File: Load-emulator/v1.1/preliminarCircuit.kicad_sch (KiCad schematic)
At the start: 4 parts, among them J4 533980771, J5 532610471, J6 532610471, J7 532610471

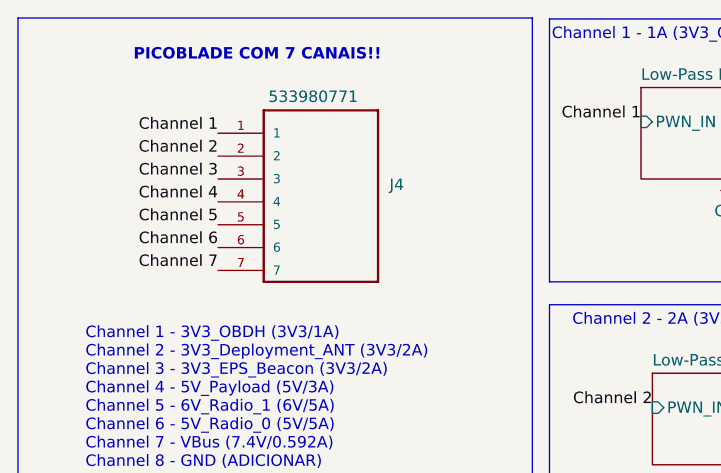
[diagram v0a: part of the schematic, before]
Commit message: changes in lib- add new connectors
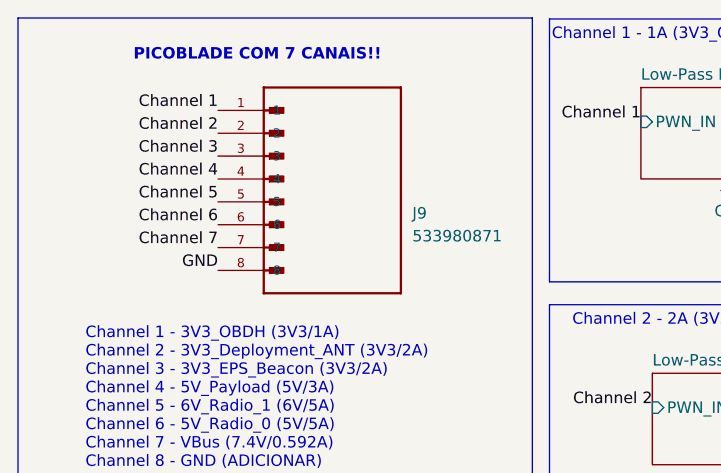
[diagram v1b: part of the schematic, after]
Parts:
- removed J4: 533980771, Connector_Molex:Molex_PicoBlade_53398-0771_1x07-1MP_P1.25mm_Vertical, symbol 533980771:533980771
- added J9: 533980871, footprints:MOLEX_533980871, symbol 533980871:533980871
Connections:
- net Channel 1: now also J9.1
- net Channel 2: now also J9.2
- net Channel 3: now also J9.3
- net Channel 4: now also J9.4
- net Channel 5: now also J9.5
- net Channel 6: now also J9.6
- net Channel 7: now also J9.7
- net GND: now also J9.8
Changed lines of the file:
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@@
+		)
+	)
+	(label "GND"
+		(at 36.83 41.91 180)
+		(effects
+			(font
+				(size 1.27 1.27)
+			)
+			(justify right bottom)
 		)
 	)
 	(label "Channel 7"
-		(at 36.83 41.91 180)
+		(at 36.83 39.37 180)
 		(effects
 			(font
@@
 	)
 	(label "Channel 2"
-		(at 36.83 29.21 180)
+		(at 36.83 26.67 180)
 		(effects
 			(font
@@
 	)
 	(label "Channel 5"
-		(at 36.83 36.83 180)
+		(at 36.83 34.29 180)
 		(effects
 			(font
@@
 	)
 	(label "Channel 4"
-		(at 36.83 34.29 180)
+		(at 36.83 31.75 180)
 		(effects
 			(font
@@
 	)
 	(label "Channel 6"
-		(at 36.83 39.37 180)
+		(at 36.83 36.83 180)
 		(effects
 			(font
@@
 	)
 	(label "Channel 1"
-		(at 36.83 26.67 180)
+		(at 36.83 24.13 180)
 		(effects
 			(font
@@
 	)
 	(label "Channel 3"
-		(at 36.83 31.75 180)
+		(at 36.83 29.21 180)
 		(effects
 			(font
@@
 	)
 	(symbol
-		(lib_id "533980771:533980771")
-		(at 48.26 35.56 0)
-		(unit 1)
-		(exclude_from_sim no)
-		(in_bom yes)
-		(on_board yes)
-		(dnp no)
-		(property "Reference" "J4"
-			(at 55.88 32.3849 0)
-			(effects
-				(font
-					(size 1.27 1.27)
-				)
-				(justify left)
-			)
-		)
-		(property "Value" "533980771"
-			(at 42.418 22.606 0)
-			(effects
-				(font
-					(size 1.27 1.27)
-				)
-				(justify left)
-			)
-		)
-		(property "Footprint" "Connector_Molex:Molex_PicoBlade_53398-0771_1x07-1MP_P1.25mm_Vertical"
-			(at 65.024 84.582 0)
-			(effects
-				(font
-					(size 1.27 1.27)
-				)
-				(justify bottom)
-				(hide yes)
-			)
-		)
-		(property "Datasheet" ""
-			(at 48.26 35.56 0)
-			(effects
-				(font
-					(size 1.27 1.27)
-				)
-				(hide yes)
-			)
-		)
-		(property "Description" ""
-			(at 48.26 35.56 0)
-			(effects
-				(font
-					(size 1.27 1.27)
-				)
-				(hide yes)
-			)
-		)
-		(property "MF" "Molex"
-			(at 81.788 48.26 0)
-			(effects
-				(font
-					(size 1.27 1.27)
-				)
-				(justify bottom)
-				(hide yes)
-			)
-		)
-		(property "MAXIMUM_PACKAGE_HEIGHT" "4.7 mm"
-			(at 65.532 33.528 0)
-			(effects
-				(font
-					(size 1.27 1.27)
-				)
-				(justify bottom)
-				(hide yes)
-			)
-		)
-		(property "Package" "None"
-			(at 65.024 29.21 0)
-			(effects
-				(font
-					(size 1.27 1.27)
-				)
-				(justify bottom)
-				(hide yes)
-			)
-		)
-		(property "Price" "None"
-			(at 68.326 27.432 0)
-			(effects
-				(font
-					(size 1.27 1.27)
-				)
-				(justify bottom)
-				(hide yes)
-			)
-		)
-		(property "Check_prices" "https://www.snapeda.com/parts/533980771/Molex/view-part/?ref=eda"
-			(at 67.818 90.424 0)
-			(effects
-				(font
-					(size 1.27 1.27)
-				)
-				(justify bottom)
-				(hide yes)
-			)
-		)
-		(property "STANDARD" "Manufacturer Recommendations"
-			(at 92.964 44.196 0)
-			(effects
-				(font
-					(size 1.27 1.27)
-				)
-				(justify bottom)
-				(hide yes)
-			)
-		)
-		(property "PARTREV" "A"
-			(at 64.262 24.384 0)
-			(effects
-				(font
-					(size 1.27 1.27)
-				)
-				(justify bottom)
-				(hide yes)
-			)
-		)
-		(property "SnapEDA_Link" "https://www.snapeda.com/parts/533980771/Molex/view-part/?ref=snap"
-			(at 50.292 74.93 0)
-			(effects
-				(font
-					(size 1.27 1.27)
-				)
-				(justify bottom)
-				(hide yes)
-			)
-		)
-		(property "MP" "533980771"
-			(at 80.518 47.498 0)
-			(effects
-				(font
-					(size 1.27 1.27)
-				)
-				(justify bottom)
-				(hide yes)
-			)
-		)
-		(property "Description_1" "\n                        \n                            Conn Shrouded Header (3 Sides) HDR 7 POS 1.25mm Solder ST Top Entry SMD PicoBlade™ T/R\n                        \n"
-			(at 48.006 67.564 0)
-			(effects
-				(font
-					(size 1.27 1.27)
-				)
-				(justify bottom)
-				(hide yes)
-			)
-		)
-		(property "Availability" "In Stock"
-			(at 74.168 59.436 0)
-			(effects
-				(font
-					(size 1.27 1.27)
-				)
-				(justify bottom)
-				(hide yes)
-			)
-		)
-		(property "MANUFACTURER" "Molex"
-			(at 65.024 34.544 0)
-			(effects
-				(font
-					(size 1.27 1.27)
-				)
-				(justify bottom)
-				(hide yes)
-			)
-		)
-		(pin "6"
-		)
-		(pin "5"
-		)
-		(pin "1"
-		)
-		(pin "2"
-		)
-		(pin "3"
-		)
-		(pin "4"
-		)
-		(pin "7"
-		)
-		(instances
-			(project ""
-				(path "/9054bfd2-3cc0-4c96-aa71-abdb09b76dc7/a12c045f-372a-4c5b-93d1-0c234b5f9c5c"
-					(reference "J4")
-					(unit 1)
-				)
-			)
-		)
-	)
-	(symbol
 		(lib_id "power:GND")
 		(at 113.03 176.53 0)
@@
 					(unit 1)
 				)
+			)
+		)
+	)
+	(symbol
+		(lib_id "533980871:533980871")
+		(at 49.53 36.83 0)
+		(unit 1)
+		(exclude_from_sim no)
+		(in_bom yes)
+		(on_board yes)
+		(dnp no)
+		(fields_autoplaced yes)
+		(property "Reference" "J9"
+			(at 58.42 35.5599 0)
+			(effects
+				(font
+					(size 1.27 1.27)
+				)
+				(justify left)
+			)
+		)
+		(property "Value" "533980871"
+			(at 58.42 38.0999 0)
+			(effects
+				(font
+					(size 1.27 1.27)
+				)
+				(justify left)
+			)
+		)
+		(property "Footprint" "footprints:MOLEX_533980871"
+			(at 61.976 1.778 0)
+			(effects
+				(font
+					(size 1.27 1.27)
+				)
+				(justify bottom)
+				(hide yes)
+			)
+		)
+		(property "Datasheet" ""
+			(at 49.53 36.83 0)
+			(effects
+				(font
+					(size 1.27 1.27)
+				)
+				(hide yes)
+			)
+		)
+		(property "Description" ""
+			(at 49.53 36.83 0)
+			(effects
+				(font
+					(size 1.27 1.27)
+				)
+				(hide yes)
+			)
+		)
+		(property "MF" "Molex"
+			(at 68.072 -7.874 0)
+			(effects
+				(font
+					(size 1.27 1.27)
+				)
+				(justify bottom)
+				(hide yes)
+			)
+		)
+		(property "MAXIMUM_PACKAGE_HEIGHT" "4.7 mm"
+			(at 57.15 1.778 0)
+			(effects
+				(font
+					(size 1.27 1.27)
+				)
+				(justify bottom)
+				(hide yes)
+			)
+		)
+		(property "Package" "None"
+			(at 71.882 -7.112 0)
+			(effects
+				(font
+					(size 1.27 1.27)
+				)
+				(justify bottom)
+				(hide yes)
+			)
+		)
+		(property "Price" "None"
+			(at 51.562 -0.508 0)
+			(effects
+				(font
+					(size 1.27 1.27)
+				)
+				(justify bottom)
+				(hide yes)
+			)
+		)
+		(property "Check_prices" "https://www.snapeda.com/parts/533980871/Molex/view-part/?ref=eda"
+			(at 35.052 -0.254 0)
+			(effects
+				(font
+					(size 1.27 1.27)
+				)
+				(justify bottom)
+				(hide yes)
+			)
+		)
+		(property "STANDARD" "Manufacturer Recommendations"
+			(at 60.452 -0.254 0)
+			(effects
+				(font
+					(size 1.27 1.27)
+				)
+				(justify bottom)
+				(hide yes)
+			)
+		)
+		(property "PARTREV" "A"
+			(at 54.356 6.604 0)
+			(effects
+				(font
+					(size 1.27 1.27)
+				)
+				(justify bottom)
+				(hide yes)
+			)
+		)
+		(property "SnapEDA_Link" "https://www.snapeda.com/parts/533980871/Molex/view-part/?ref=snap"
+			(at 35.052 -0.254 0)
+			(effects
+				(font
+					(size 1.27 1.27)
+				)
+				(justify bottom)
+				(hide yes)
+			)
+		)
+		(property "MP" "533980871"
+			(at 52.832 4.572 0)
+			(effects
+				(font
+					(size 1.27 1.27)
+				)
+				(justify bottom)
+				(hide yes)
+			)
+		)
+		(property "Description_1" "Connector Header Surface Mount 8 position 0.049 (1.25mm)"
+			(at 35.052 -0.254 0)
+			(effects
+				(font
+					(size 1.27 1.27)
+				)
+				(justify bottom)
+				(hide yes)
+			)
+		)
+		(property "Availability" "In Stock"
+			(at 55.118 3.556 0)
+			(effects
+				(font
+					(size 1.27 1.27)
+				)
+				(justify bottom)
+				(hide yes)
+			)
+		)
+		(property "MANUFACTURER" "Molex"
+			(at 66.294 -7.62 0)
+			(effects
+				(font
+					(size 1.27 1.27)
+				)
+				(justify bottom)
+				(hide yes)
+			)
+		)
+		(pin "4"
+		)
+		(pin "6"
+		)
+		(pin "1"
+		)
+		(pin "2"
+		)
+		(pin "3"
+		)
+		(pin "5"
+		)
+		(pin "8"
+		)
+		(pin "7"
+		)
+		(instances
+			(project "Load-emulator"
+				(path "/9054bfd2-3cc0-4c96-aa71-abdb09b76dc7/a12c045f-372a-4c5b-93d1-0c234b5f9c5c"
+					(reference "J9")
+					(unit 1)
+				)

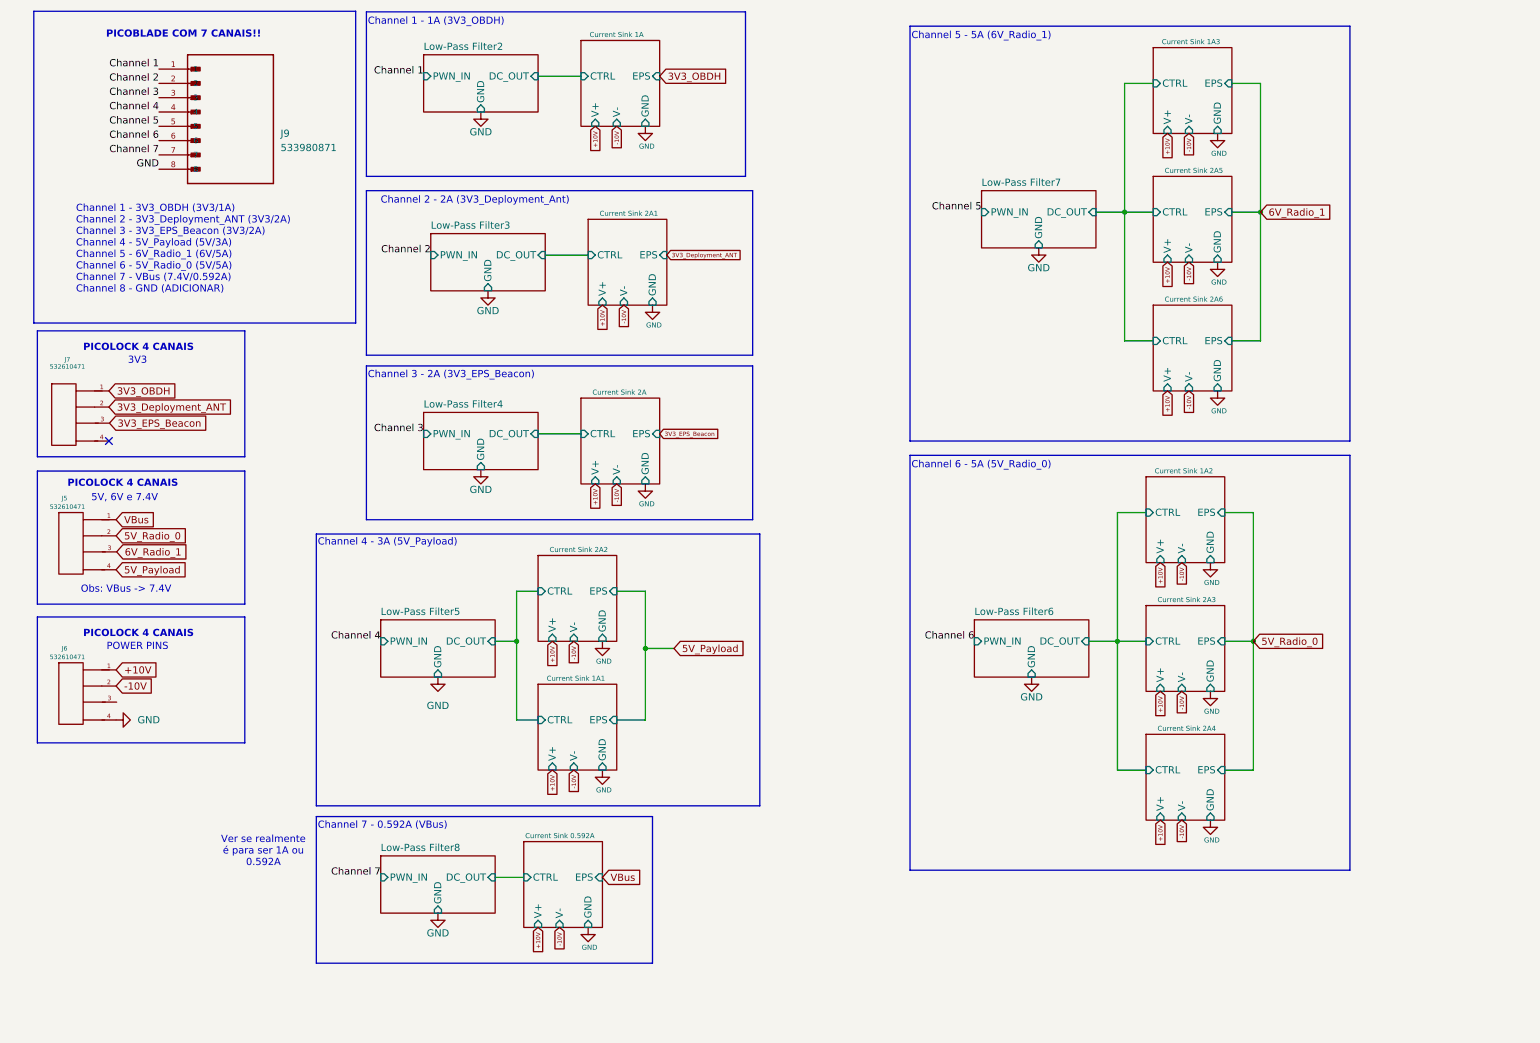
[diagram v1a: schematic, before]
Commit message: Channels reduced to 3A max
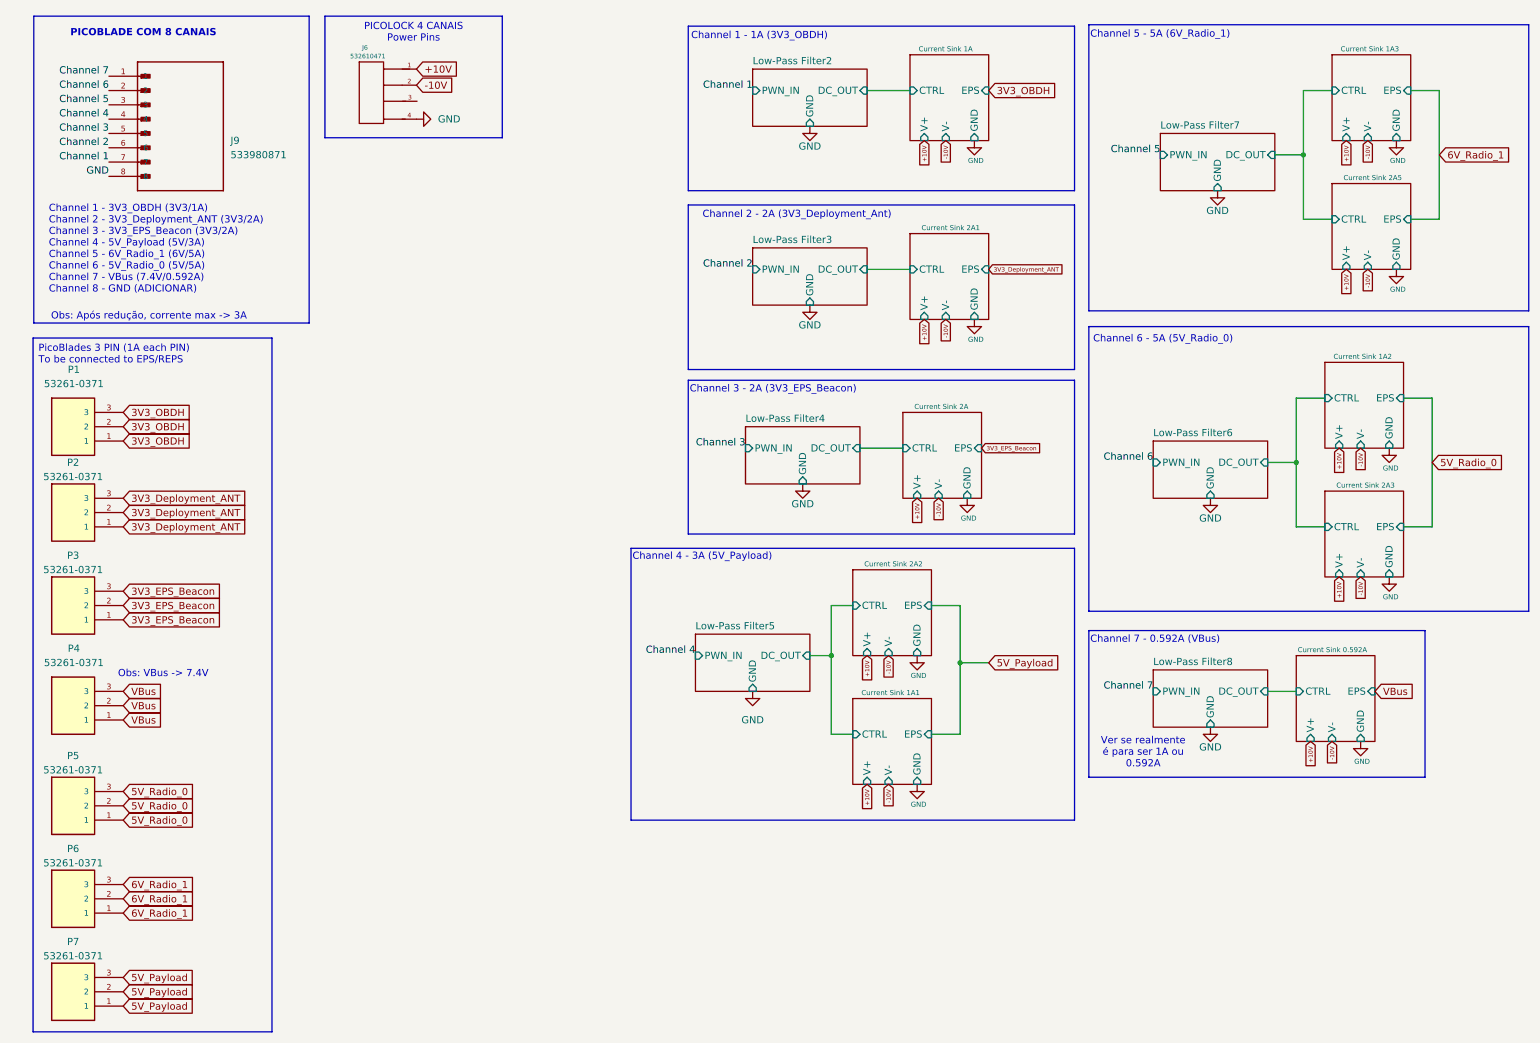
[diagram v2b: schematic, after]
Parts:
- removed J5, J7: 532610471, footprints:532610471, symbol 532610471:532610471
- added P1, P2, P3, P4, P5, P6, P7: 53261-0371, footprints:MOLEX_53261-0371, symbol 53261-0371:53261-0371
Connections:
- net 3V3_Deployment_ANT: now also P2.1, P2.2, P2.3
- net 3V3_EPS_Beacon: now also P3.1, P3.2, P3.3
- net 3V3_OBDH: now also P1.1, P1.2, P1.3
- net 5V_Payload: now also P7.1, P7.2, P7.3
- net 5V_Radio_0: now also P5.1, P5.2, P5.3
- net 6V_Radio_1: now also P6.1, P6.2, P6.3
- net Channel 1: now also J9.7; no longer J9.1
- net Channel 2: now also J9.6; no longer J9.2
- net Channel 3: now also J9.5; no longer J9.3
- net Channel 5: now also J9.3; no longer J9.5
- net Channel 6: now also J9.2; no longer J9.6
- net Channel 7: now also J9.1; no longer J9.7
- net VBus: now also P4.1, P4.2, P4.3
- no-connect marks 1 -> 0
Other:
- removed sheet Current Sink 2A4
- removed sheet Current Sink 2A6
- note added: "Obs: Após redução, corrente max -> 3A"
- note added: "PICOBLADE COM 8 CANAIS"
- note removed: "3V3"
- note removed: "5V, 6V e 7.4V"
- note removed: "PICOBLADE COM 7 CANAIS!!"
- note removed: "PICOLOCK 4 CANAIS"
- note removed: "POWER PINS"
- moved on the sheet: J6, J9

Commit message: Foram adicionados todos os canais, removidos os pinos de conexao para o REPS, foram feitas todas as trilhas de potência, controle e alimentação, com exceção do GND.
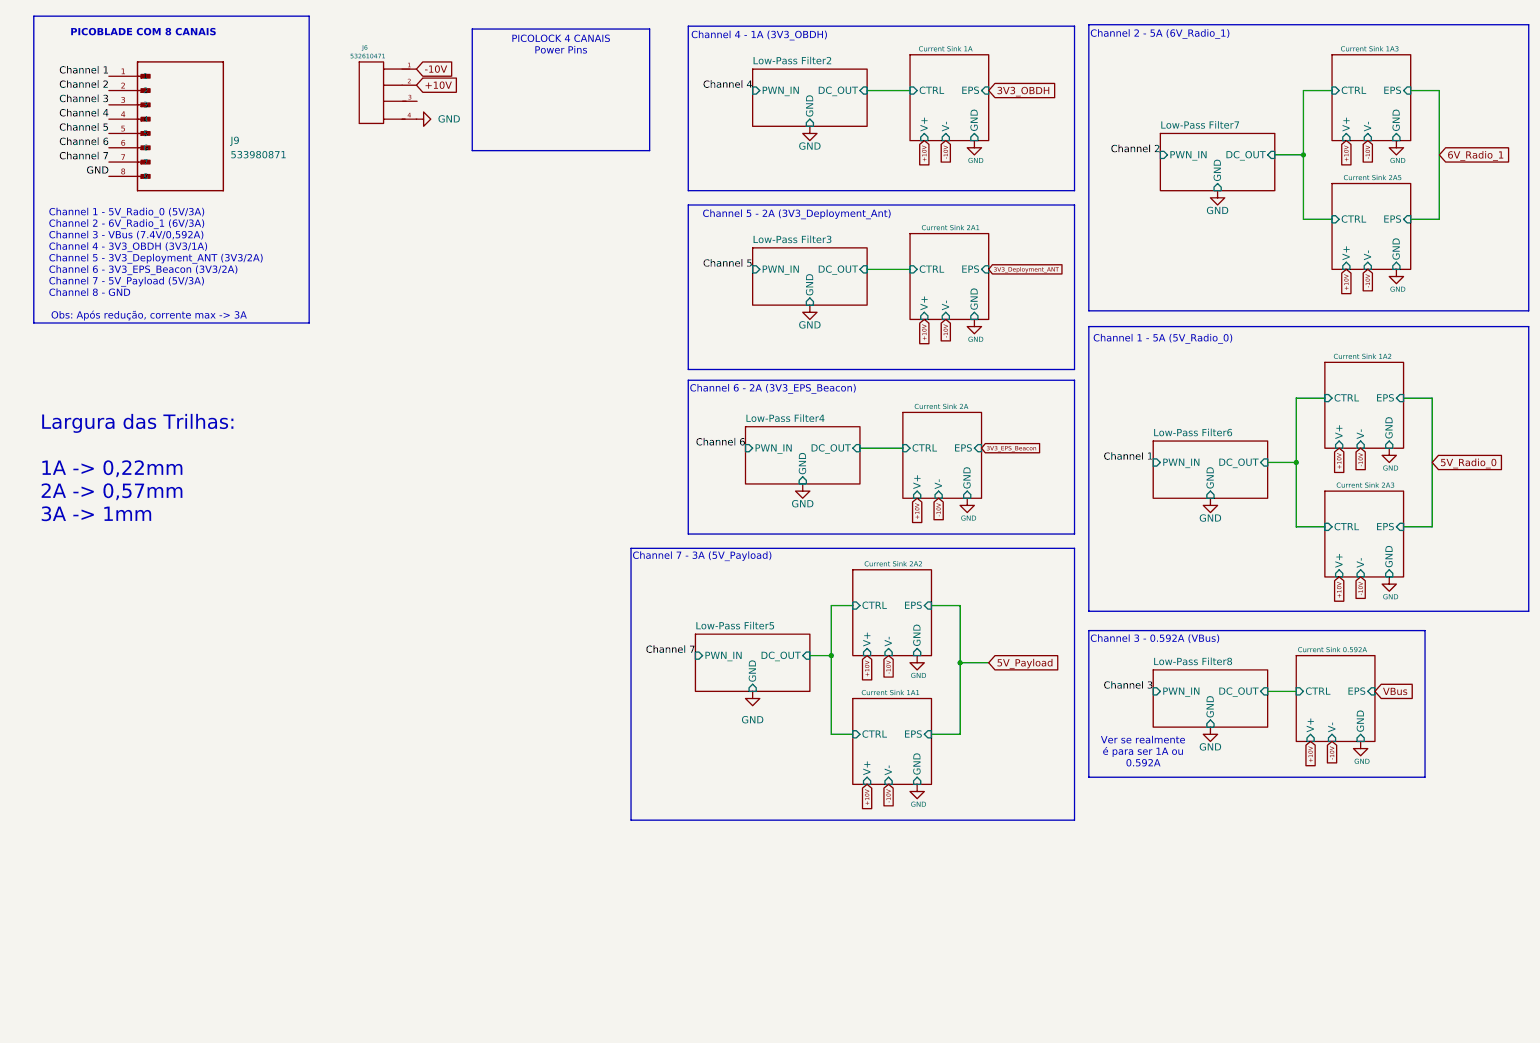
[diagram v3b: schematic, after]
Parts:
- removed P1, P2, P3, P4, P5, P6, P7: 53261-0371, footprints:MOLEX_53261-0371, symbol 53261-0371:53261-0371
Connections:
- net +10V: now also J6.2; no longer J6.1
- net -10V: now also J6.1; no longer J6.2
- net Channel 1: now also J9.1; no longer J9.7
- net Channel 2: now also J9.2; no longer J9.6
- net Channel 3: now also J9.3; no longer J9.5
- net Channel 5: now also J9.5; no longer J9.3
- net Channel 6: now also J9.6; no longer J9.2
- net Channel 7: now also J9.7; no longer J9.1
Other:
- note added: "Channel 1 - 5A (5V_Radio_0)"
- note added: "Channel 1 - 5V_Radio_0 (5V/3A) Channel 2 - 6V_Radio_1 (6V/3A) Channel 3 - VBus (7.4V/0,592A) Channel 4 - 3V3_OBDH (3V3/1A) Channel 5 - 3V3_Deployment_ANT (3V3/2A) Channel 6 - 3V3_EPS_Beacon (3V3/2A) Channel 7 - 5V_Payload (5V/3A) Channel 8 - GND"
- note added: "Channel 2 - 5A (6V_Radio_1)"
- note added: "Channel 3 - 0.592A (VBus)"
- note added: "Channel 4 - 1A (3V3_OBDH)"
- note added: "Channel 5 - 2A (3V3_Deployment_Ant)"
- note added: "Channel 6 - 2A (3V3_EPS_Beacon)"
- note added: "Channel 7 - 3A (5V_Payload)"
- note added: "Largura das Trilhas: 1A -> 0,22mm 2A -> 0,57mm 3A -> 1mm"
- note removed: "Channel 1 - 1A (3V3_OBDH)"
- note removed: "Channel 1 - 3V3_OBDH (3V3/1A) Channel 2 - 3V3_Deployment_ANT (3V3/2A) Channel 3 - 3V3_EPS_Beacon (3V3/2A) Channel 4 - 5V_Payload (5V/3A) Channel 5 - 6V_Radio_1 (6V/5A) Channel 6 - 5V_Radio_0 (5V/5A) Channel 7 - VBus (7.4V/0.592A) Channel 8 - GND (ADICIONAR)"
- note removed: "Channel 2 - 2A (3V3_Deployment_Ant)"
- note removed: "Channel 3 - 2A (3V3_EPS_Beacon)"
- note removed: "Channel 4 - 3A (5V_Payload)"
- note removed: "Channel 5 - 5A (6V_Radio_1)"
- note removed: "Channel 6 - 5A (5V_Radio_0)"
- note removed: "Channel 7 - 0.592A (VBus)"
- note removed: "Obs: VBus -> 7.4V"
